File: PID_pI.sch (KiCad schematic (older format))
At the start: 34 parts

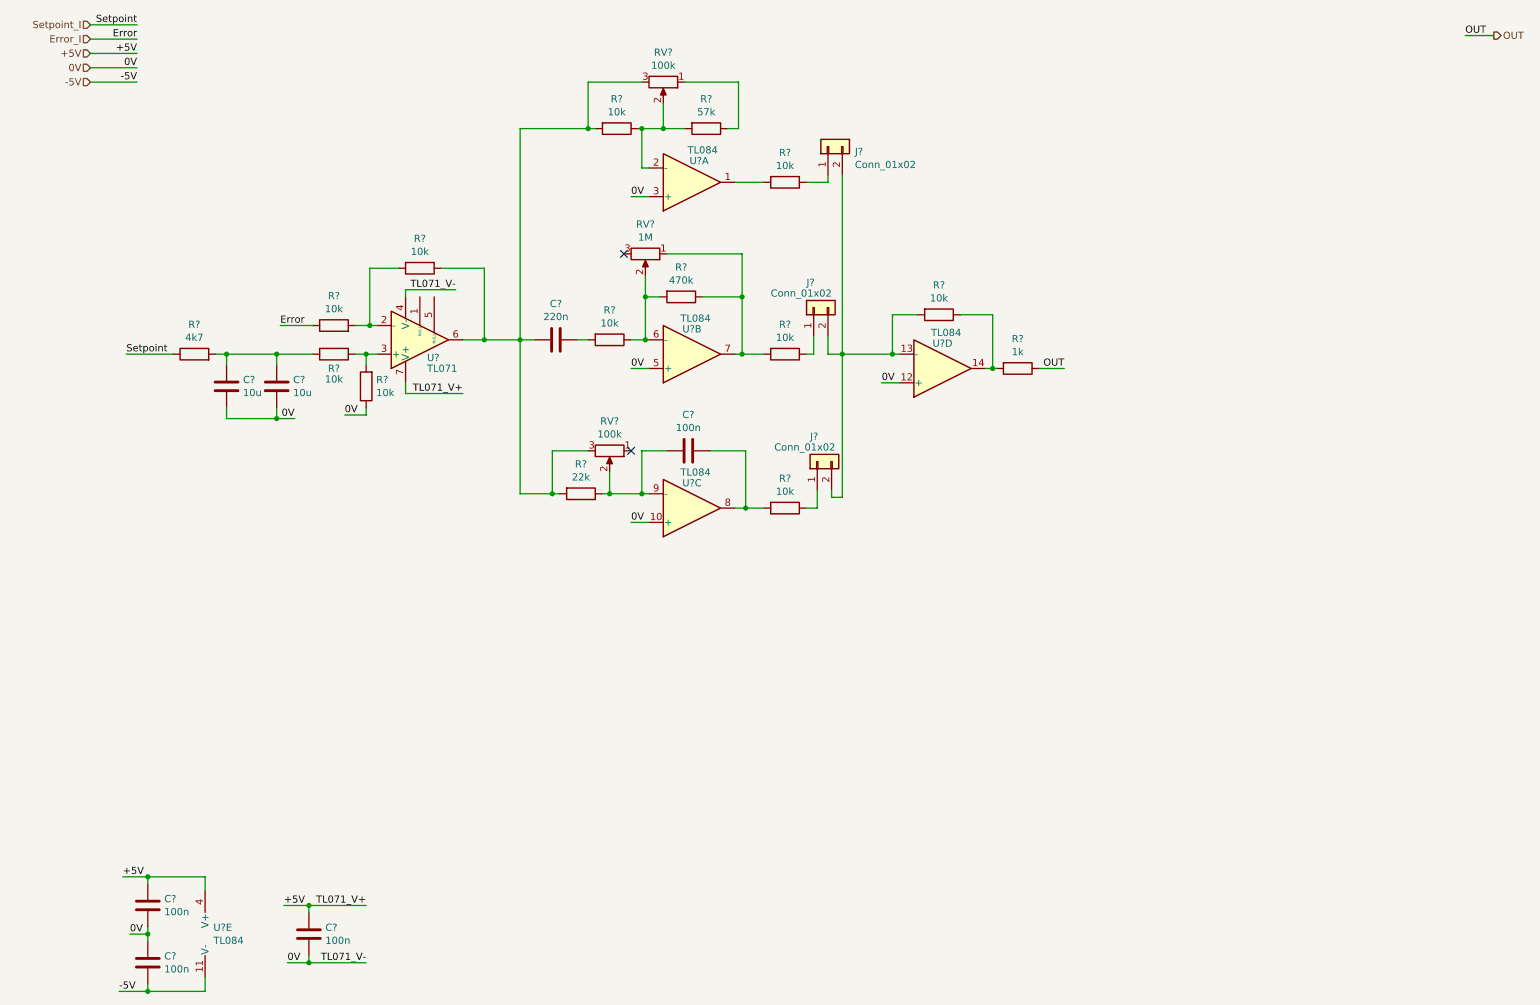
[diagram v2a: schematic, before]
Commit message: Added integrator reset, fixed Switch.sch
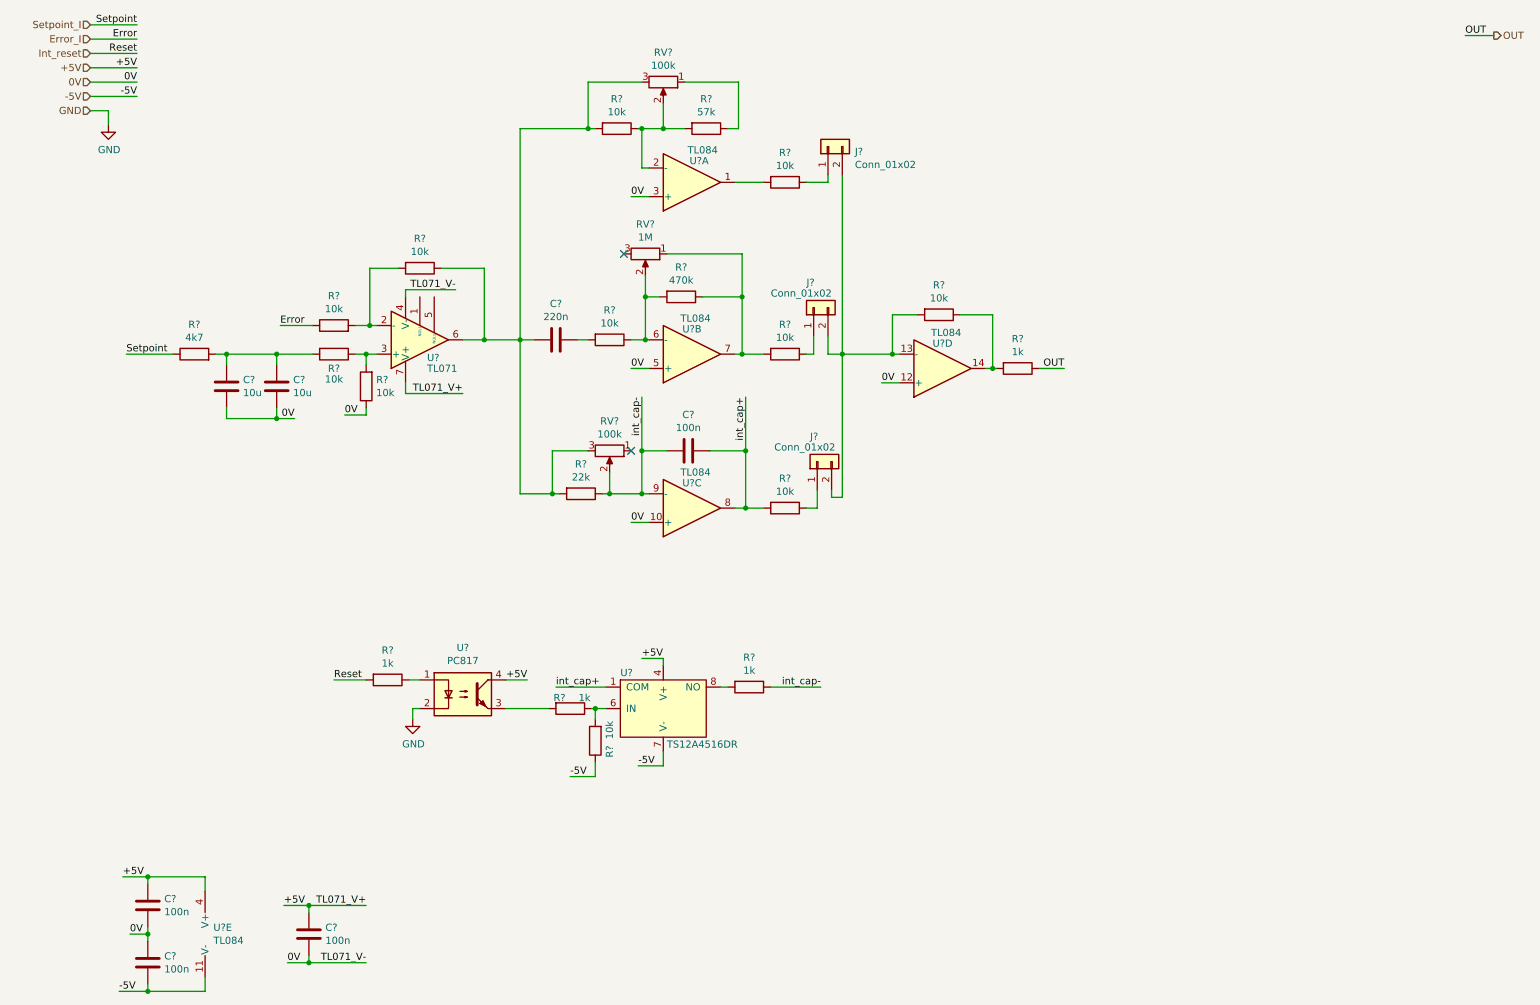
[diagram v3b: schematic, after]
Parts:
- removed C? (x4): 100n, symbol Device:C
- removed C?: 10u, symbol Device:C
- removed R? (x5): 10k, symbol Device:R
- removed R?: 57k, symbol Device:R
- removed R?: 470k, symbol Device:R
- removed R?: 22k, symbol Device:R
- removed U? (x5): TL084, symbol Amplifier_Operational:TL084
- removed U?: TL071, symbol Amplifier_Operational:TL071
- added C? (x4): 100n, symbol Device:C
- added C?: 10u, symbol Device:C
- added R? (x3): 1k, symbol Device:R
- added R? (x6): 10k, symbol Device:R
- added R?: 57k, symbol Device:R
- added R?: 470k, symbol Device:R
- added R?: 22k, symbol Device:R
- added U?: TS12A4516DR, symbol Lib:TS12A4516DR
- added U?: PC817, Package_DIP:DIP-4_W7.62mm, symbol Isolator:PC817
- added U? (x5): TL084, symbol Amplifier_Operational:TL084
- added U?: TL071, symbol Amplifier_Operational:TL071
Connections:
- net +5V: now also C?.1, C?.1, U?.4, U?.4 (V+), U?.4 (V+), U?.7 (V+)
- net -5V: now also C?.2, R?.1, U?.11 (V-), U?.7 (V-)
- net 0V: now also C?.1, C?.1, C?.2, C?.2, R?.1, U?.10 (+), U?.12 (+), U?.3 (+), U?.4 (V-), U?.5 (+)
- net Error_I: now also R?.1
- net at R?.2: now also U?.1
- net at RV?.2: now also R?.1, R?.2, U?.2 (-)
- net at R?.1, RV?.2: now also R?.2, U?.6 (-)
- net at R?.2, RV?.1: now also R?.1, U?.7
- net int_cap-: now reaches RV?.2
- net int_cap-: now also C?.2, R?.1, R?.1, U?.9 (-)
- net at J?.2 (Pin_2), J?.2 (Pin_2), J?.2 (Pin_2)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: now also U?.13 (-)
- net at R?.1, R?.2: now also U?.14
- net at C?.2, R?.1, RV?.3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: now also R?.2, R?.2, U?.6
- net at RV?.1: now also R?.1
- net at J?.1 (Pin_1): now also R?.1
- net at R?.2: now also R?.2, U?.2 (-)
- net at C?.2, R?.2: now also C?.2, R?.2
- new net: R?.1, R?.2, U?.6 (IN)
- new net: R?.2, U?.8 (NO)
- new net: R?.1, U?.1
- new net: R?.2, U?.3
- new net: R?.1, R?.2, U?.3 (+)
- new net GND: U?.2
- new net Int_reset: R?.2
- new net int_cap+: C?.1, R?.2, U?.1 (COM), U?.8

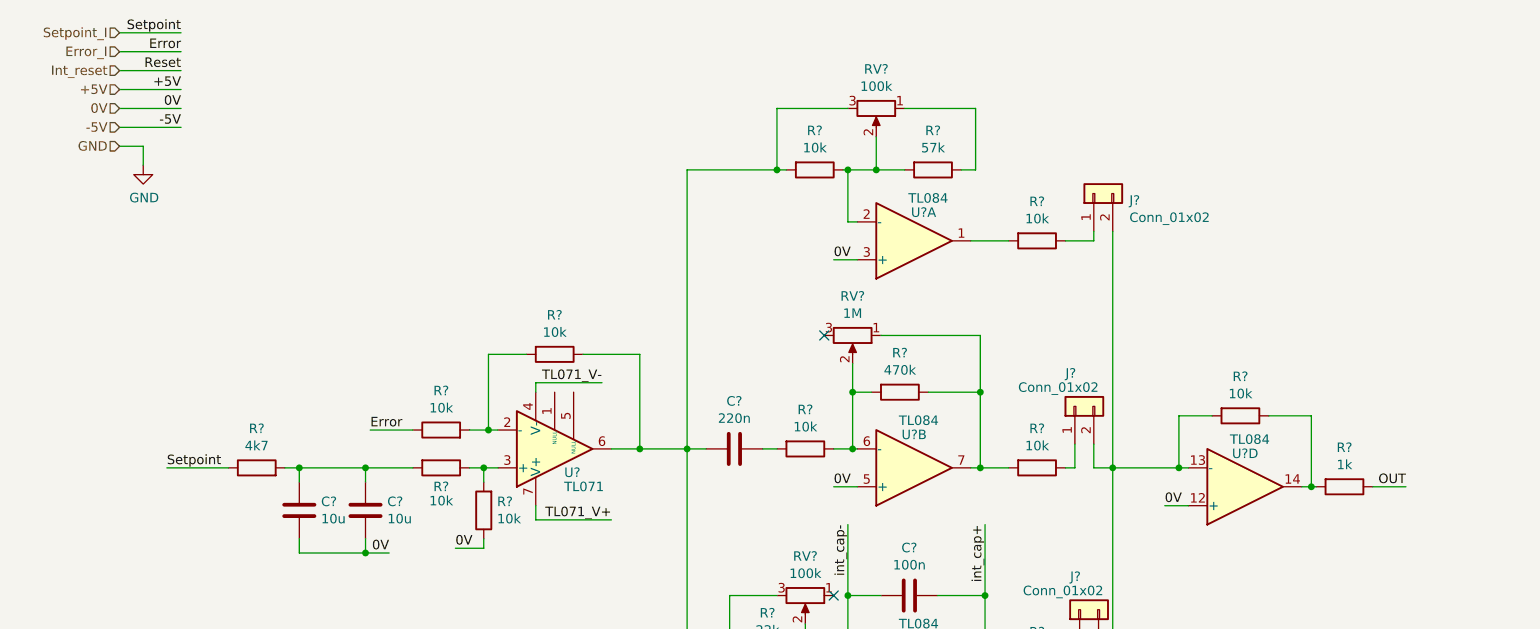
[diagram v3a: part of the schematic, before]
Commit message: Added laser diode, power stage, connecting block in progress
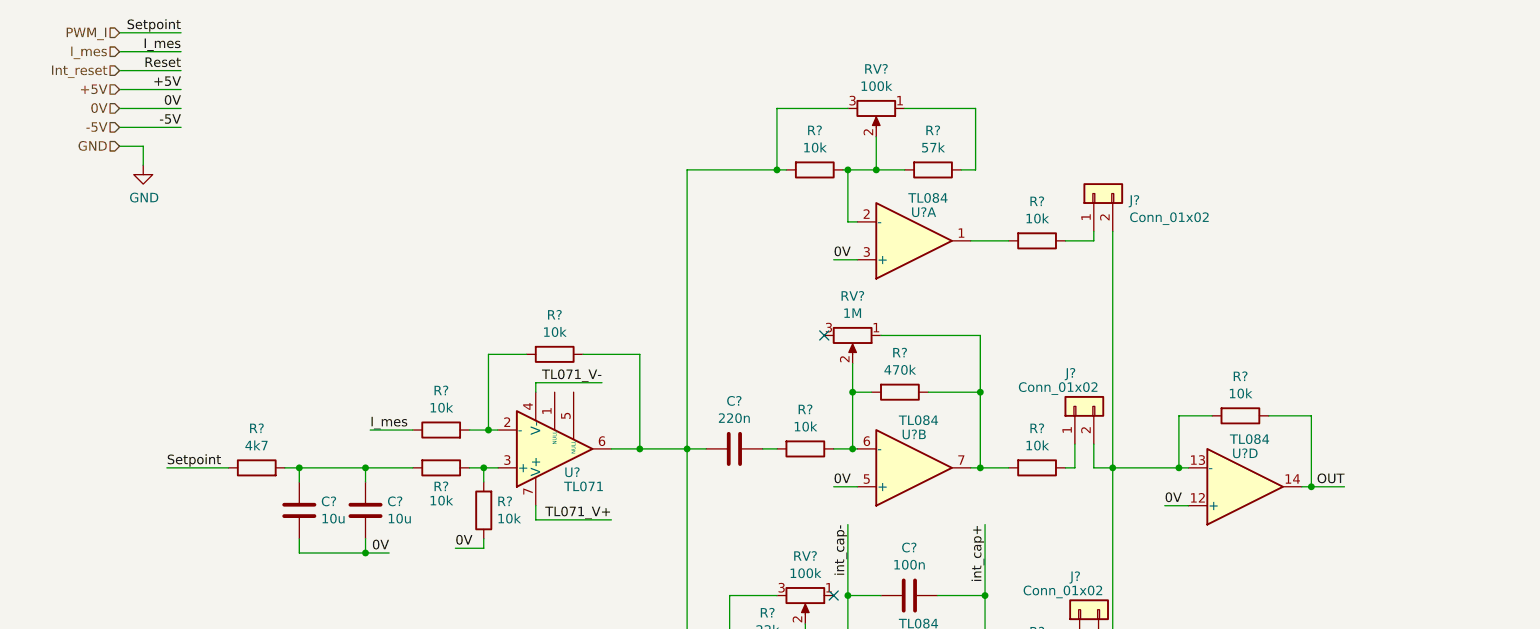
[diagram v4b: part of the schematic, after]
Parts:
- removed R?: 1k, symbol Device:R
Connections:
- net OUT: now also R?.1, U?.14
- net Error_I renamed I_mes
- net Setpoint_I renamed PWM_I
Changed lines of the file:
@@
 $Descr A4 11693 8268
 encoding utf-8
-Sheet 11 12
+Sheet 10 11
 Title ""
 Date ""
@@
 $EndComp
 Text HLabel 950  600  0    50   Input ~ 0
-Setpoint_I
+PWM_I
 Text HLabel 950  700  0    50   Input ~ 0
-Error_I
+I_mes
 Text HLabel 950  900  0    50   Input ~ 0
 +5V
@@
 Wire Wire Line
 	6475 3100 6600 3100
-$Comp
-L Device:R R?
-U 1 1 619938D0
-P 7425 3000
-AR Path="/619B51F3/619938D0" Ref="R?"  Part="1"
-AR Path="/61820F6B/619938D0" Ref="R?"  Part="1"
-AR Path="/61A28785/619938D0" Ref="R?"  Part="1"
-AR Path="/61A63B19/619938D0" Ref="R?"  Part="1"
-AR Path="/619BC68D/619938D0" Ref="R?"  Part="1"
-AR Path="/619C27A2/619938D0" Ref="R?"  Part="1"
-AR Path="/619C2E9F/619938D0" Ref="R?"  Part="1"
-AR Path="/619C995F/619938D0" Ref="R?"  Part="1"
-F 0 "R?" V 7218 3000 50  0000 C CNN
-F 1 "1k" V 7309 3000 50  0000 C CNN
-F 2 "" V 7355 3000 50  0001 C CNN
-F 3 "~" H 7425 3000 50  0001 C CNN
-	1    7425 3000
-	0    1    1    0
-$EndComp
-Wire Wire Line
-	7275 3000 7250 3000
 Connection ~ 7250 3000
-Text Label 7750 3000 2    50   ~ 0
+Text Label 7425 3000 2    50   ~ 0
 OUT
-Wire Wire Line
-	7750 3000 7575 3000
 Text Label 10550 675  0    50   ~ 0
 OUT
@@
 Wire Wire Line
 	1275 600  950  600
-Text Label 1275 700  2    50   ~ 0
-Error
 Wire Wire Line
 	1275 700  950  700
 Text Label 2275 2700 0    50   ~ 0
-Error
+I_mes
 Text Label 1200 2900 0    50   ~ 0
 Setpoint
@@
 Wire Wire Line
 	3850 5375 4150 5375
+Wire Wire Line
+	7250 3000 7425 3000
+Text Label 1275 700  2    50   ~ 0
+I_mes
 $EndSCHEMATC
